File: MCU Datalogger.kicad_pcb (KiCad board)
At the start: 2 copper layers, 50.8 x 30.5 mm, 29 parts, among them J1 Conn_01x09_Pin, J2 Conn_01x04_Pin, J3 Conn_01x04_Pin, J4 Conn_02x03_Odd_Even, U1 DS1337S_, U2 24LC1025, U3 24LC1025, U4 ATMEGA328P-AU, Y1 32.768 KHz, Y2 16 MHz

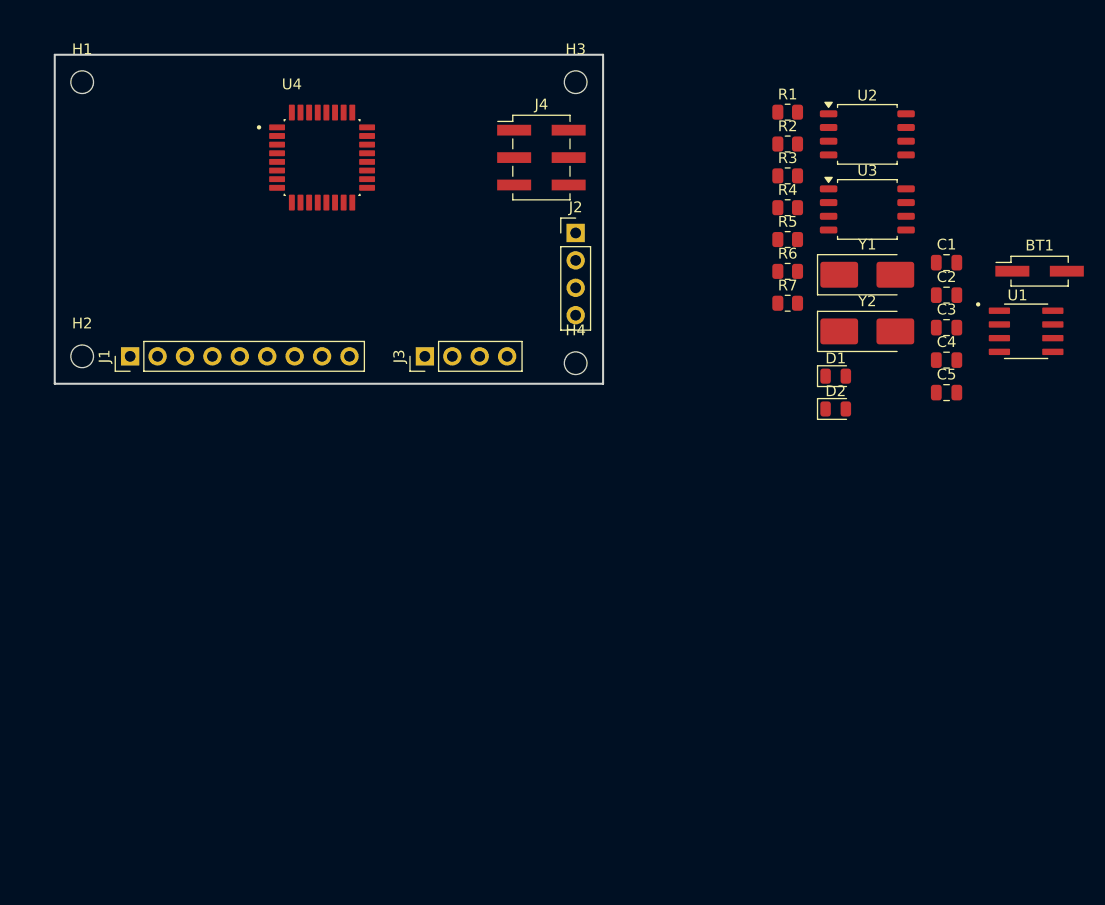
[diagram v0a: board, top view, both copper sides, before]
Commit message: arrange component on layout
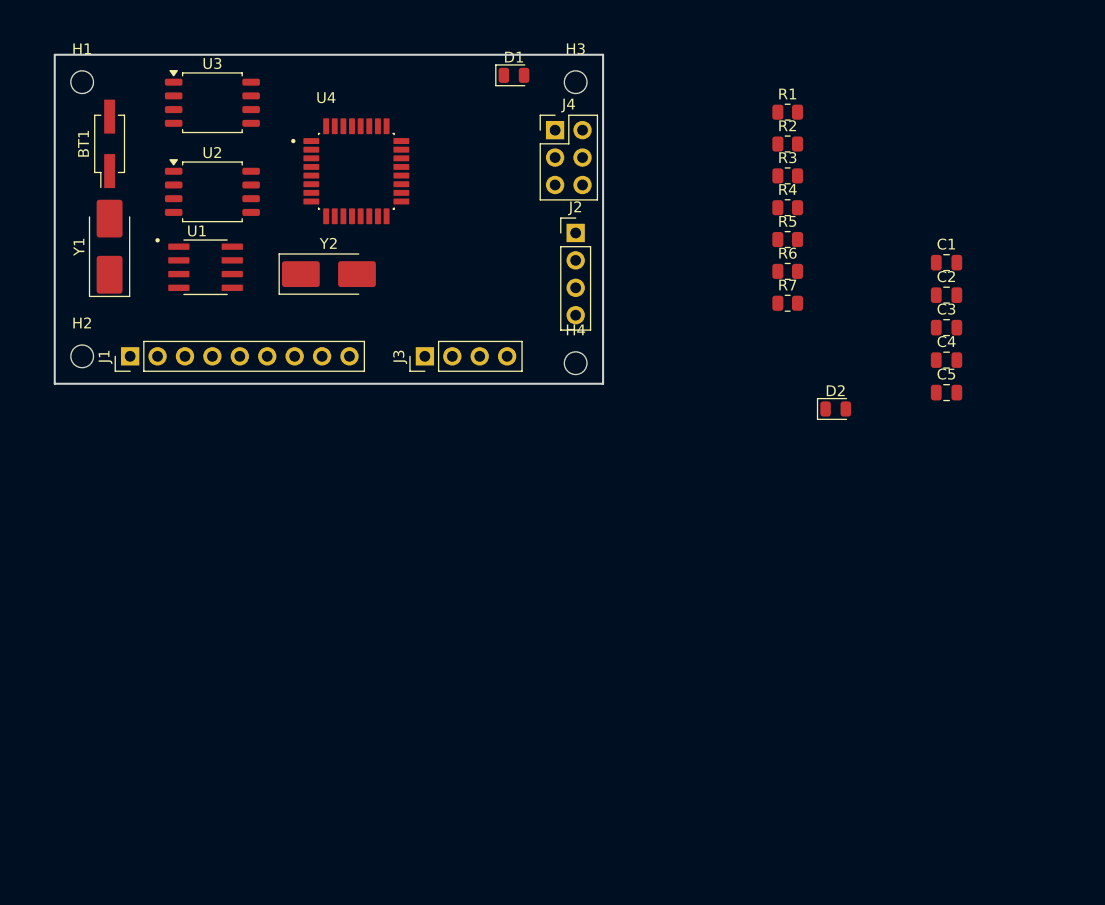
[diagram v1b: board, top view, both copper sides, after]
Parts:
- J4: footprint Connector_PinHeader_2.54mm:PinHeader_2x03_P2.54mm_Vertical_SMD -> Connector_PinHeader_2.54mm:PinHeader_2x03_P2.54mm_Vertical
- moved BT1 87.0 mm to (99.1, 99.7), turned to 90 degrees
- moved U1 76.3 mm to (108.0, 111.1)
- moved Y1 70.2 mm to (99.1, 109.2), turned to 90 degrees
- moved U3 61.5 mm to (108.6, 95.9)
- moved U2 60.9 mm to (108.6, 104.1)
- moved Y2 50.2 mm to (119.4, 111.8)
- moved D1 40.8 mm to (136.5, 93.3)
- moved U4 3.42 mm to (121.9, 102.2)
- moved J4 2.84 mm to (140.3, 98.4)

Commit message: finish routing
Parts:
- BT1: footprint Connector_PinHeader_2.54mm:PinHeader_2x01_P2.54mm_Vertical_SMD -> Connector_PinHeader_2.54mm:PinHeader_2x01_P2.54mm_Vertical
- moved C1 63.3 mm to (115.6, 94.0)
- moved C3 61.6 mm to (119.4, 94.0)
- moved C5 60.7 mm to (123.2, 94.0)
- moved R1 58.3 mm to (106.7, 115.6)
- moved R2 53.8 mm to (110.5, 115.6), turned to 180 degrees
- moved C4 48.5 mm to (128.9, 111.1), turned to 180 degrees
- moved D2 48.1 mm to (128.9, 94.0)
- moved C2 48.0 mm to (128.9, 108.0), turned to 180 degrees
- moved R7 37.5 mm to (128.3, 97.8)
- moved R4 33.4 mm to (128.9, 100.3), turned to 180 degrees
- moved R3 33.0 mm to (128.9, 104.1), turned to 180 degrees
- moved R5 30.7 mm to (133.3, 97.2), turned to 180 degrees
- moved R6 30.2 mm to (133.3, 101.6)
- moved H1 3.59 mm to (94.0, 91.4)
- moved H2 3.59 mm to (94.0, 121.9)
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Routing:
- net /SCK: track 0.00 -> 101.7 mm, vias 0 -> 1
- net /VCC: track 0.00 -> 94.2 mm, vias 0 -> 3
- net GND: track 0.00 -> 89.7 mm, vias 0 -> 11
- net /SDA: track 0.00 -> 65.2 mm, vias 0 -> 2
- net Net-(BT1-+): track 0.00 -> 57.4 mm, vias 0 -> 5
- net /D2: track 0.00 -> 34.9 mm, vias 0 -> 1
- net /D4: track 0.00 -> 32.3 mm, vias 0 -> 2
- net /TX: track 0.00 -> 30.0 mm, vias 0 -> 1
- net /D3: track 0.00 -> 28.5 mm, vias 0 -> 2
- net /RX: track 0.00 -> 26.2 mm, vias 0 -> 1
- net Net-(U4-PB7): track 0.00 -> 25.4 mm, vias 0 -> 2
- net /MOSI: track 0.00 -> 23.1 mm
- net Net-(U4-PB6): track 0.00 -> 22.9 mm
- net /RESET: track 0.00 -> 22.8 mm, vias 0 -> 4
- net /MISO: track 0.00 -> 19.1 mm, vias 0 -> 1
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- added copper zone on F.Cu, net /VCC
- added copper zone on B.Cu, net GND
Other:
- board size 50.8 x 30.5 mm -> 56.9 x 36.6 mm
- board text added: "+"
- board text added: "-"
- board text added: "2"
- board text added: "3"
- board text added: "4"
- board text added: "5"
- board text added: "6"
- board text added: "7"
- board text added: "8"
- board text added: "GND"
- board text added: "I2C"
- board text added: "ICSP"
- board text added: "RX"
- board text added: "SCK"
- board text added: "SDA"
- board text added: "TX"
- board text added: "VCC"

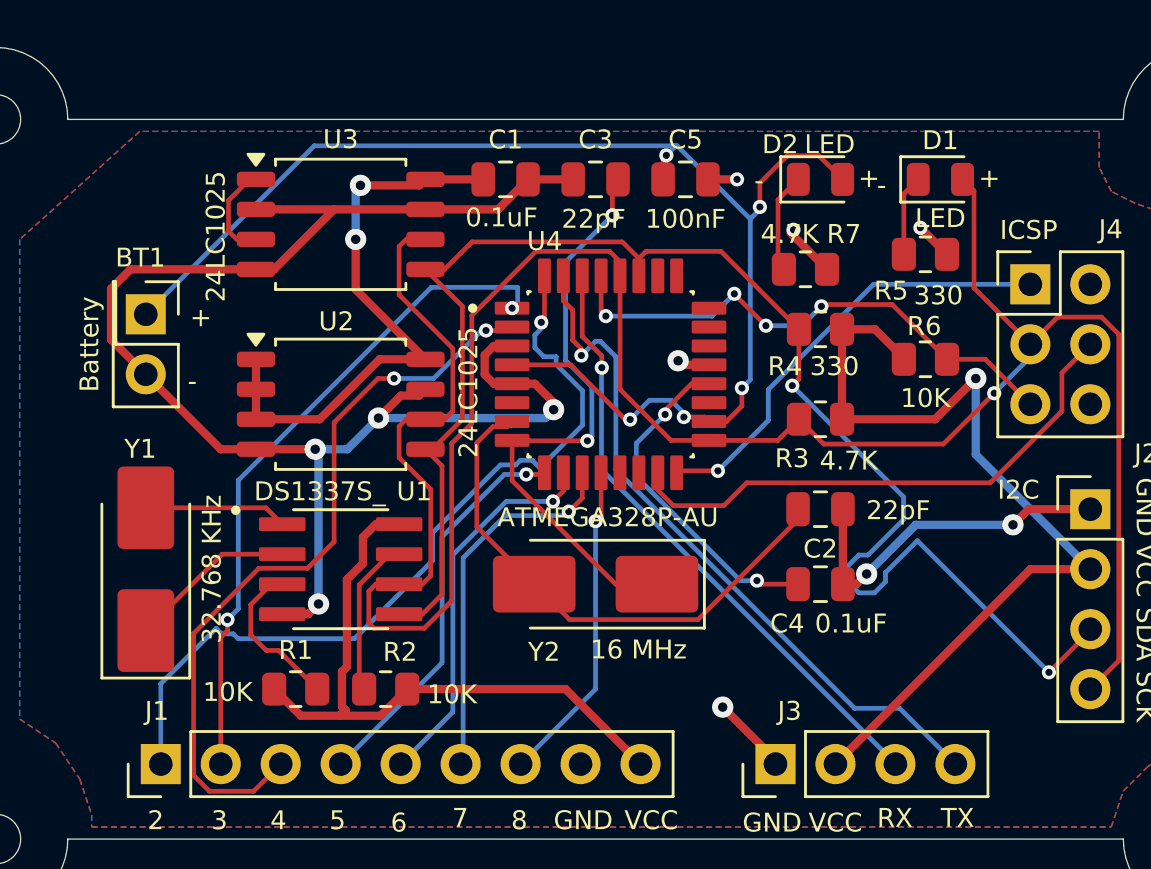
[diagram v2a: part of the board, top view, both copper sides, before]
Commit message: finish 2 layer route
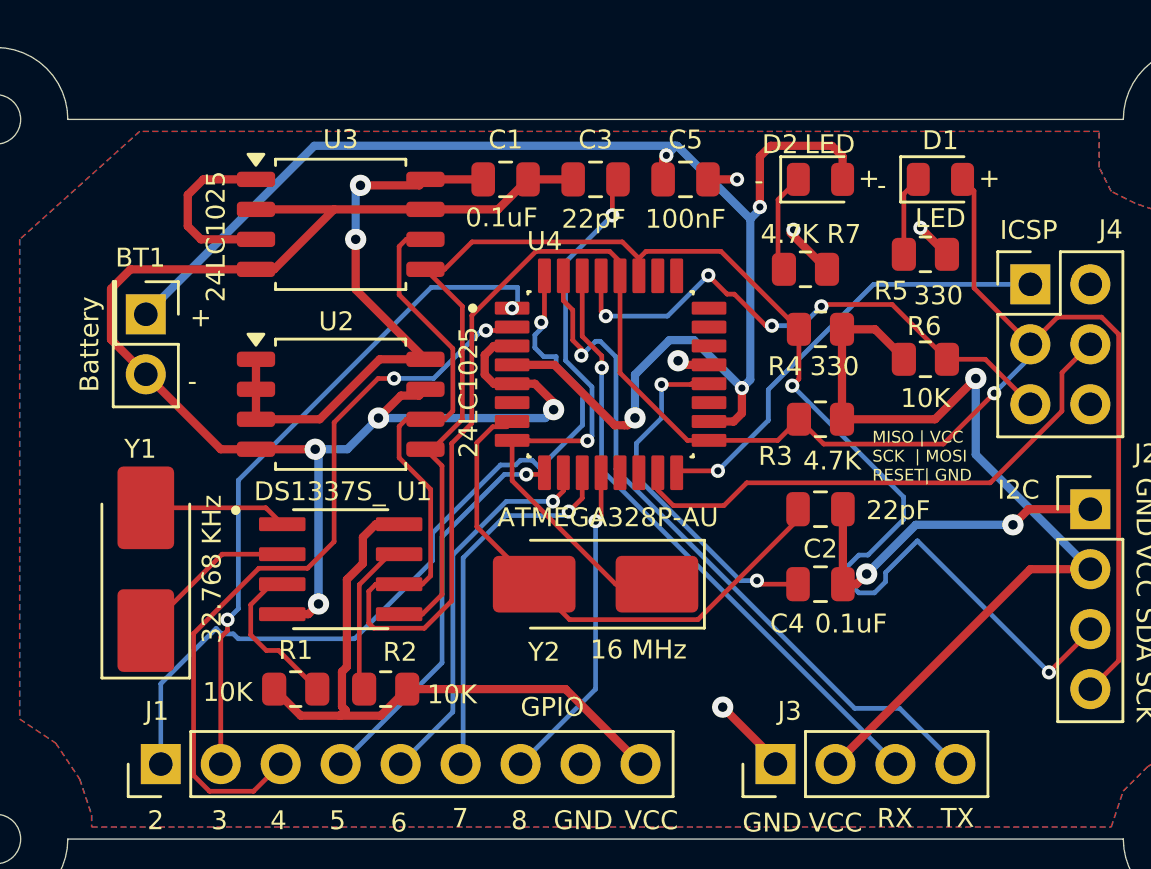
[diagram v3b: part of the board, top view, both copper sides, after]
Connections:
- BT1 pad 1: Net-(BT1-+) -> /VCC
- C5 pad 1: Net-(BT1-+) -> /VCC
- D2 pad 2: Net-(BT1-+) -> /VCC
- U4 pad 18: Net-(BT1-+) -> /VCC
- U4 pad 4: Net-(BT1-+) -> /VCC
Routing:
- net /VCC: track 94.2 -> 160.9 mm, vias 3 -> 7
- net Net-(BT1-+): track 57.4 -> 0.00 mm, vias 5 -> 0
- net Net-(U4-AREF): track 14.4 -> 15.1 mm
- net /RESET: track 22.8 -> 23.5 mm
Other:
- board text added: "GPIO"
- board text added: "MISO | VCC SCK | MOSI RESET| GND"

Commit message: finish 2 layer
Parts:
- added REF**: KiCad-Logo2_5mm_SilkScreen, Symbol:KiCad-Logo2_5mm_SilkScreen, B.Cu at (115.8, 144.3)
- moved BT1 43.6 mm to (106.0, 142.9)
- moved C4 43.6 mm to (134.6, 154.3)
- moved H1 43.6 mm to (99.7, 134.6)
- moved H3 43.6 mm to (150.5, 134.6)
- moved J1 43.6 mm to (106.7, 161.9)
- moved J3 43.6 mm to (132.7, 161.9)
- moved R1 43.6 mm to (112.4, 158.8)
- moved R2 43.6 mm to (116.2, 158.8)
- moved R5 43.6 mm to (139.1, 140.3)
- moved R6 43.6 mm to (139.1, 144.8)
- moved U2 43.6 mm to (114.3, 146.7)
- moved Y2 43.6 mm to (125.1, 154.3)
- moved C1 43.6 mm to (121.3, 137.2)
- moved C2 43.6 mm to (134.6, 151.1)
- moved C3 43.6 mm to (125.1, 137.2)
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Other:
- board text added: "- 2MBit EEPROM - RTC - I2C, SPI, GPIOS"
- board text added: "0.0000 mm / 0.0000 mm"
- board text added: "0.3000 mm"
- board text added: "1.6000 mm"
- board text added: "56.9000 mm x 36.5800 mm"
- board text added: "BOARD CHARACTERISTICS"
- board text added: "Board Thickness:"
- board text added: "Board overall dimensions:"
- board text added: "Castellated pads:"
- board text added: "Copper Finish:"
- board text added: "Copper Layer Count:"
- board text added: "Data logger with the ATMega328P."
- board text added: "Edge card connectors:"
- board text added: "Impedance Control:"
- board text added: "Min hole diameter:"
- board text added: "Min track/spacing:"
- board text added: "No"
- board text added: "None"
- board text added: "Plated Board Edge:"

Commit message: finish 4 layer pcb
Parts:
- moved J1 1.27 mm to (108.0, 161.9)
- moved Y2 1.04 mm to (126.1, 154.3)
- moved R1 0.63 mm to (112.4, 158.1)
- moved R2 0.63 mm to (116.2, 158.1)
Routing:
- net GND: track 89.7 -> 39.5 mm, vias 11 -> 13
- net /VCC: track 160.9 -> 112.3 mm, vias 7 -> 12
- net /SCK: track 101.3 -> 92.7 mm, vias 1 -> 5
- net /SDA: track 65.2 -> 57.2 mm, vias 2 -> 5
- net /D4: track 32.3 -> 24.6 mm, vias 2 -> 0
- net /D8: track 13.8 -> 20.4 mm, vias 1 -> 0
- net /RX: track 26.2 -> 30.6 mm, vias 1 -> 0
- net /TX: track 30.0 -> 33.6 mm, vias 1 -> 0
- net /MISO: track 19.1 -> 22.0 mm
- net /D2: track 34.9 -> 32.1 mm, vias 1 -> 0
- net Net-(U4-AREF): track 15.1 -> 17.3 mm
- net /D7: track 16.0 -> 14.1 mm, vias 1 -> 0
- net Net-(U1-~{INTA}): track 6.74 -> 5.00 mm
- net /RESET: track 23.5 -> 21.9 mm, vias 4 -> 2
- net Net-(U4-PB7): track 25.4 -> 23.9 mm, vias 2 -> 3
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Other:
- copper layers 2 -> 4

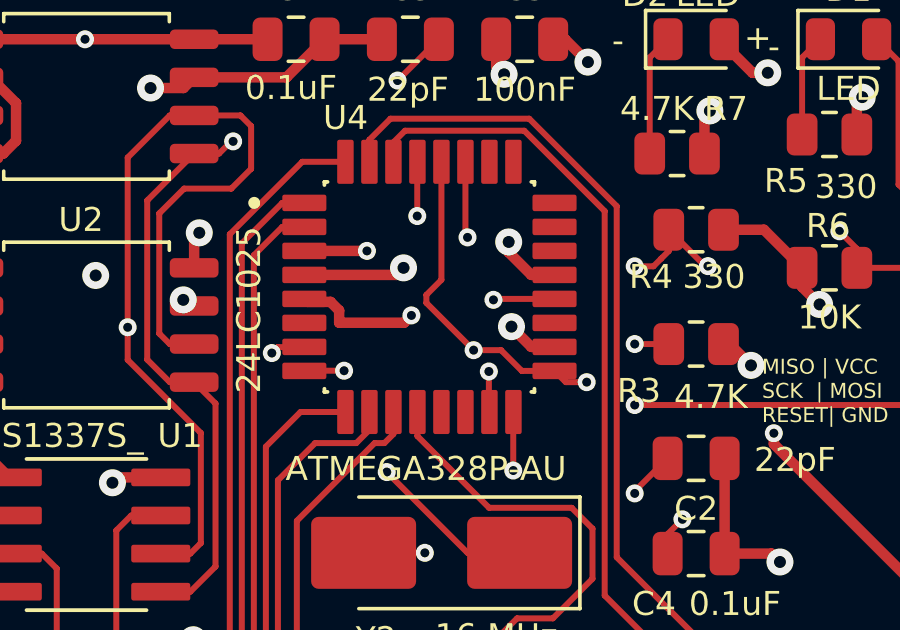
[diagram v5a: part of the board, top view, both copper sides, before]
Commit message: merge schematics to change
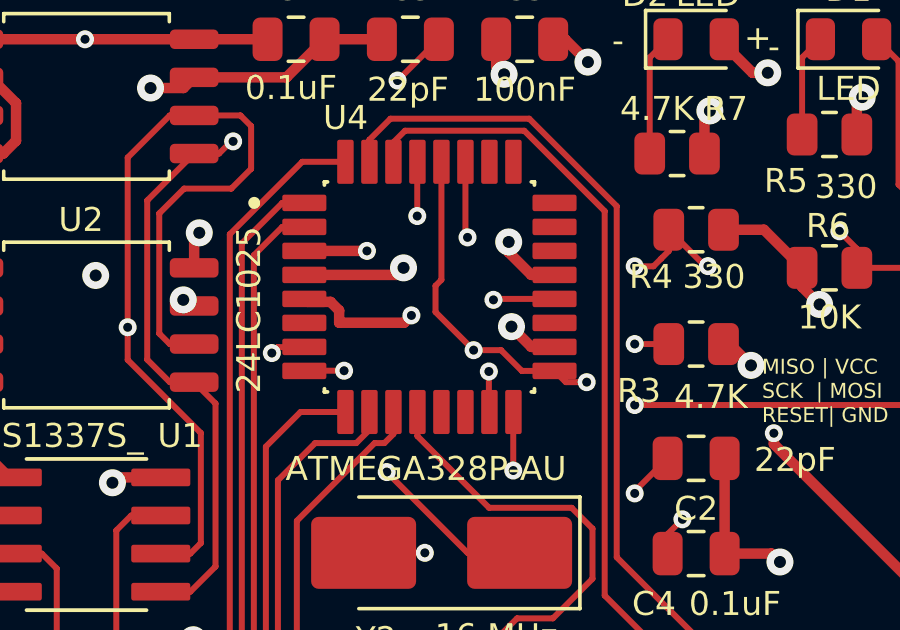
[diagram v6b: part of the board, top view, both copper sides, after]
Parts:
- removed REF**: KiCad-Logo2_5mm_SilkScreen, Symbol:KiCad-Logo2_5mm_SilkScreen

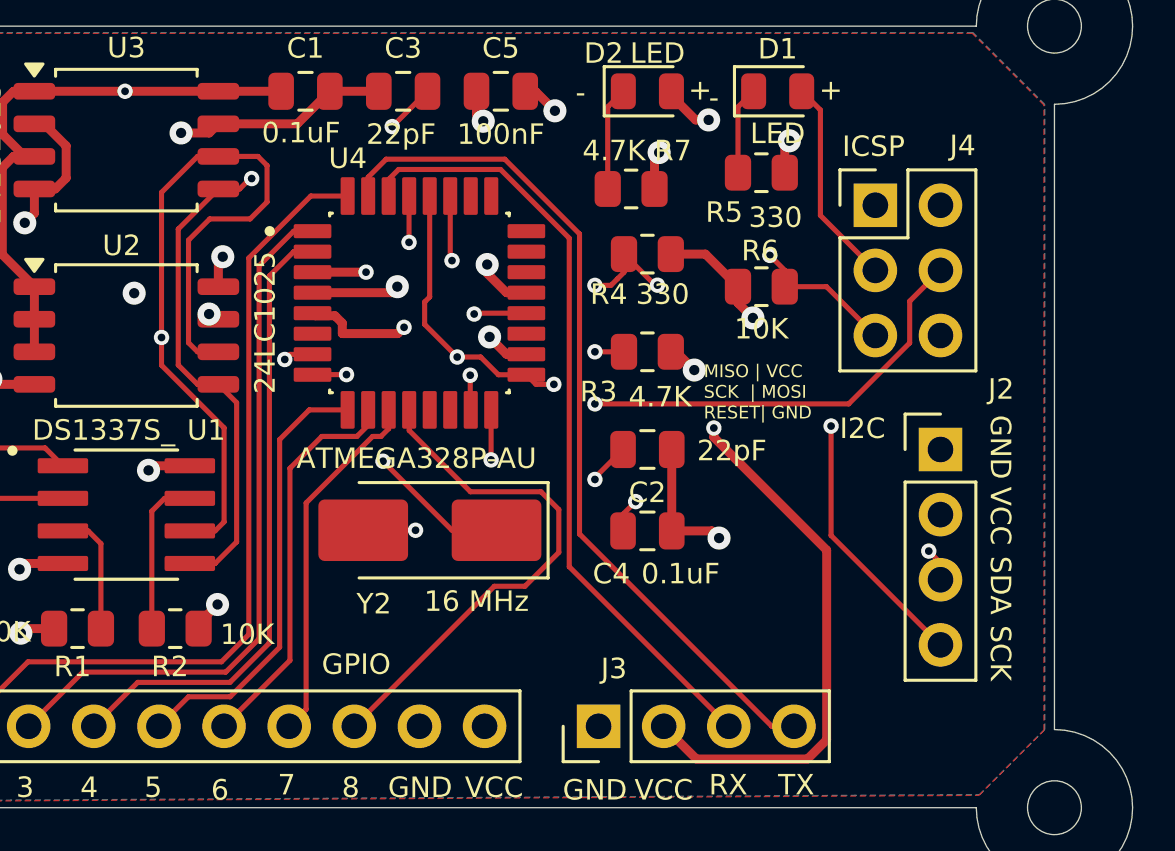
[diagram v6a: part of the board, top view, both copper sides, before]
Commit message: update SCL connection
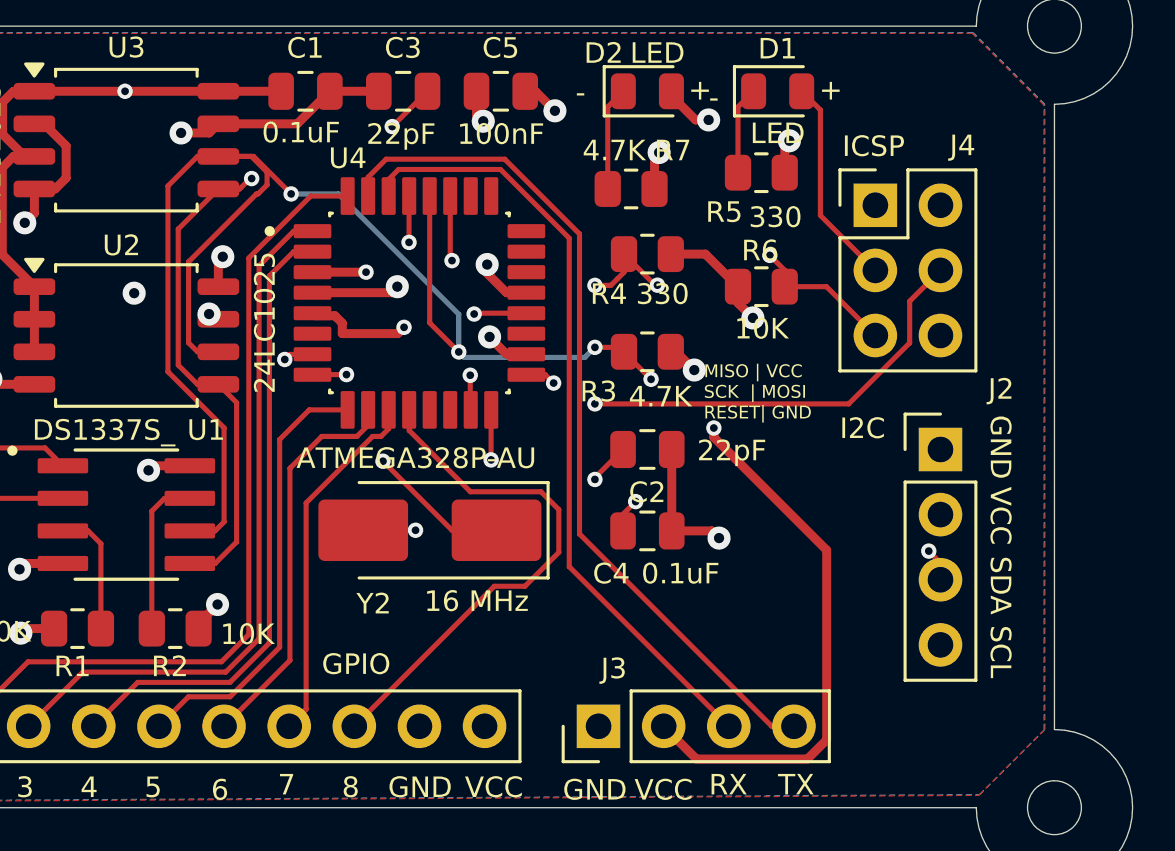
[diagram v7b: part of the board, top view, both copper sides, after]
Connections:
- net Net-(U4-AREF) renamed /Abc123
- J2 pad 4: /SCK -> /SCL
- R3 pad 2: /SCK -> /SCL
- U1 pad 6: /SCK -> /SCL
- U2 pad 6: /SCK -> /SCL
- U3 pad 6: /SCK -> /SCL
- U4 pad 28: /SCK -> /SCL
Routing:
- net /SCL: track 0.00 -> 73.4 mm, vias 0 -> 4
- net /SCK: track 92.5 -> 23.7 mm, vias 5 -> 1
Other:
- board text added: "SCL"
- board text removed: "SCK"

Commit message: add custom logo
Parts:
- added G***: LOGO, verdiq_logo:Verdiq_logo_10x10_positive, B.Cu at (114.8, 154.9)
